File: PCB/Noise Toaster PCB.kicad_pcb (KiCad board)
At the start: 2 copper layers, 132.1 x 68.6 mm, 142 parts, among them J10 GND, J2 Power, J3 AREG, J4 LFO, J5 VCO, J6 VCO, J7 LPF, J8 VCA, J9 Amp, Q1 2N5457, Q10 2N3906, Q2 2N3904, Q3 2N3904, Q4 2N3904, Q5 2N3904, Q6 2N3904, Q7 2N5457, Q8 2N5457, Q9 2N5457, U1 LM324, U2 LM324, U3 LM386, X4 WNS

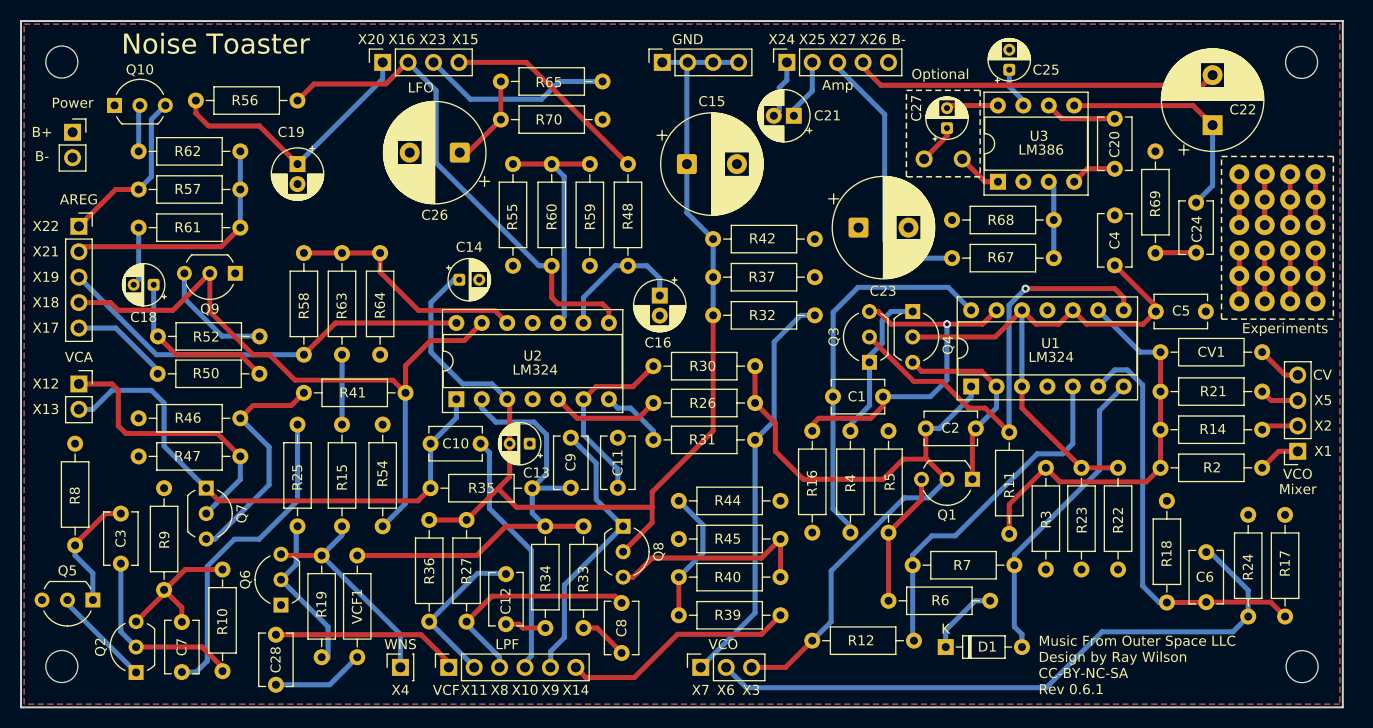
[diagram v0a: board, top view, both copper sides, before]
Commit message: Fixed grave mistake (Q10 position swapped)
Tom forgot to mirror Q10, swapping the emitter and collectors of Q10
Changed all the footprints of electrolytic caps to 5mm (i didnt find a single cap in my parts bin rated for 25V that was 4mm diameter)
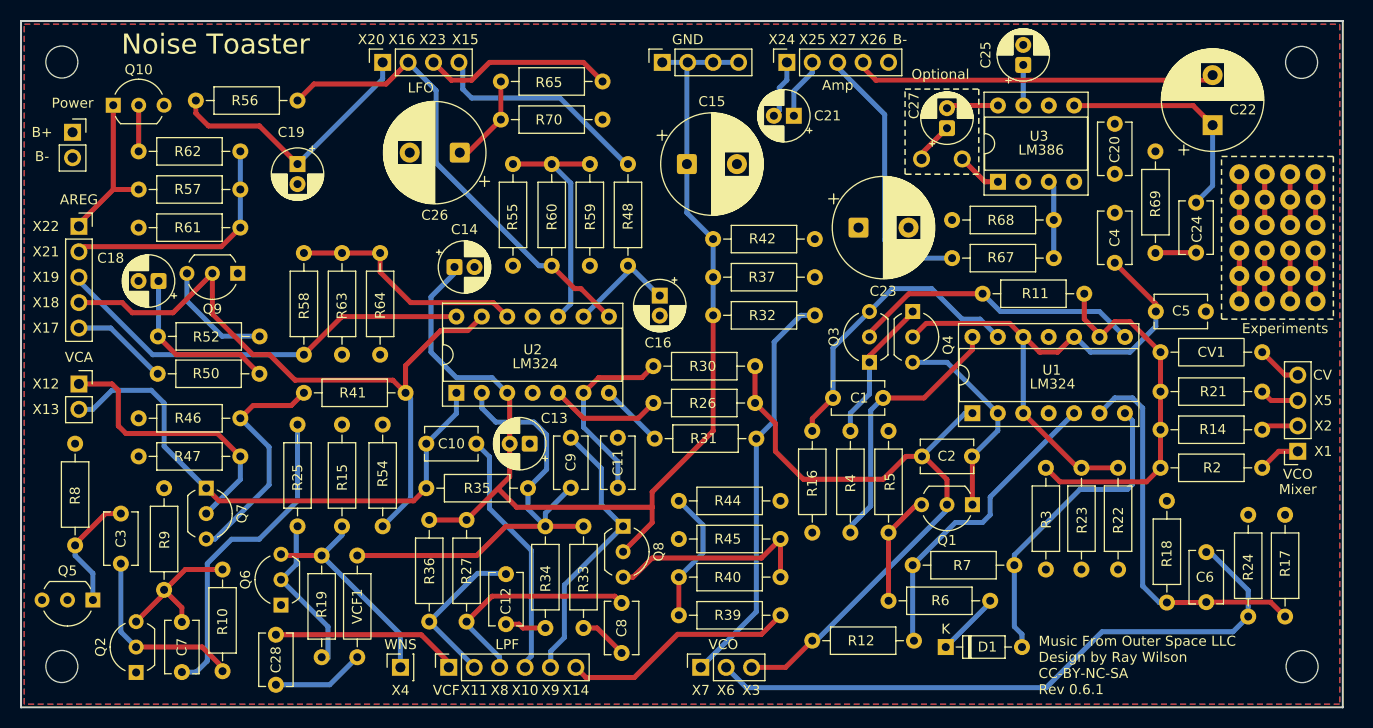
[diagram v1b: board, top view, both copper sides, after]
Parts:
- C13, C14, C18, C25, C27: footprint Capacitor_THT:CP_Radial_D4.0mm_P2.00mm -> Capacitor_THT:CP_Radial_D5.0mm_P2.00mm
- C2: value 0.001 uF -> 1 nF
- moved R11 25.1 mm to (181.5, 102.5), turned to 180 degrees
- moved C1 5.00 mm to (156.4, 112.9), turned to 0 degrees
- moved C2 2.82 mm to (170.3, 118.8)
- moved U1 2.67 mm to (170.3, 114.5)
- moved Q1 2.54 mm to (170.3, 123.6)
- moved C25 1.48 mm to (175.4, 79.7)
- moved C14 1.36 mm to (118.6, 99.8)
- moved U2 0.64 mm to (118.8, 112.4)
- moved C18 0.62 mm to (89.0, 101.2)
- moved C20 0.51 mm to (184.6, 90.5)
- moved C10 0.43 mm to (120.8, 117.5)
- moved R35 0.43 mm to (115.8, 121.9)
- moved C4 0.25 mm to (184.6, 99.4)
- moved Q9 0.25 mm to (96.9, 100.5)
- moved ? 0.25 mm to (165.3, 89.1)
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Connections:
- Q10 pad 1: B- -> /Attack Release Envelope Generator/X22
- Q10 pad 3: /Attack Release Envelope Generator/X22 -> B-
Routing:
- net B-: track 20.2 -> 0.00 mm
- net Net-(Q3-B): track 44.4 -> 29.3 mm, vias 1 -> 0
- net B+: track 14.1 -> 0.00 mm
- net Net-(C1-Pad2): track 37.9 -> 26.6 mm
- net Net-(Q3-C): track 35.2 -> 30.2 mm, vias 1 -> 0
- net /RMP: track 69.5 -> 65.3 mm
- net Net-(U1B-+): track 34.8 -> 30.9 mm
- net Net-(U1C--): track 40.2 -> 37.1 mm
- net /Front Panel/B: track 50.3 -> 47.5 mm
- net Net-(U1B--): track 41.2 -> 38.5 mm
- net Net-(U2C--): track 13.7 -> 11.1 mm
- net Net-(Q1-G): track 13.5 -> 11.3 mm
- net /Front Panel/X15: track 21.0 -> 22.5 mm
- net Net-(U2A--): track 46.4 -> 47.8 mm
- net Net-(Q3-E): track 15.1 -> 13.9 mm
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
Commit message: Final Update
Move power pins closer to filter caps
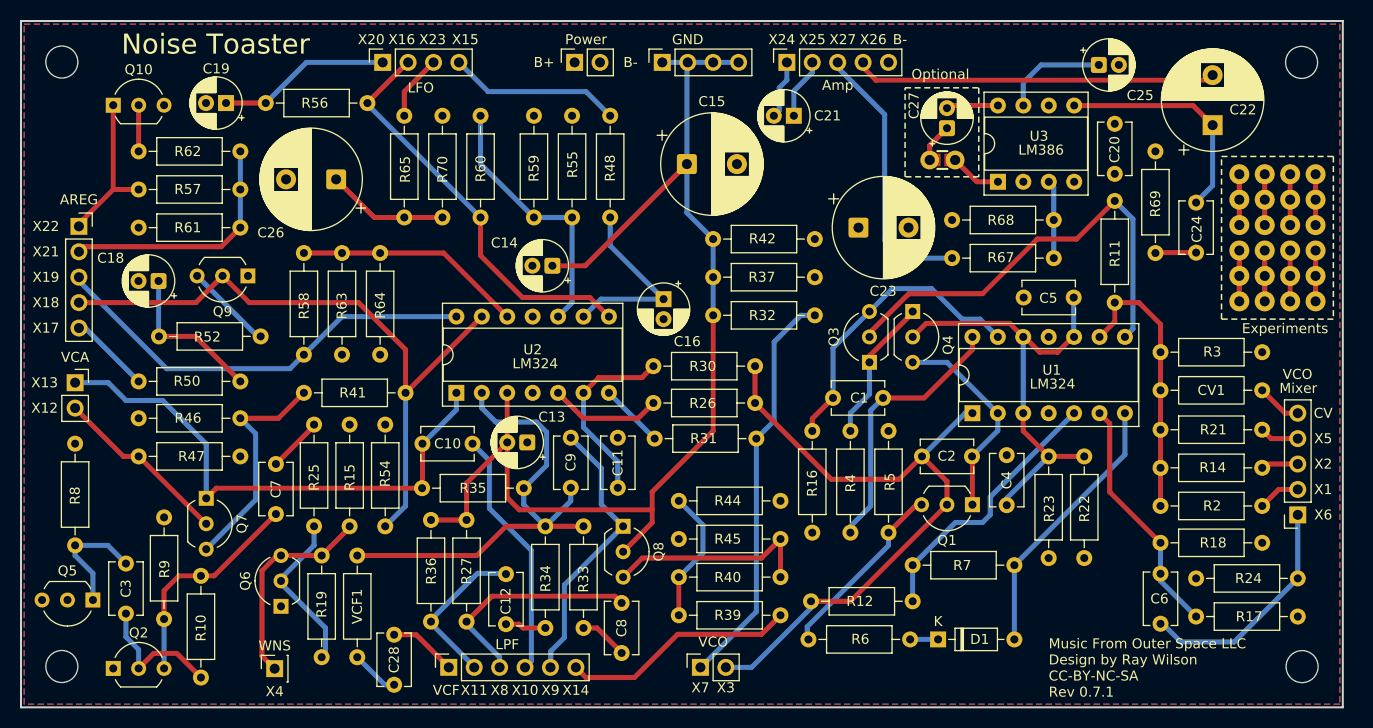
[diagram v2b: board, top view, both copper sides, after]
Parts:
- removed the ? at (169.3, 89.1)
- removed the ? at (165.3, 89.1)
- added JP1: Jumper_Measure_Open, PCM_SparkFun-Jumper:Jumper_2_PTH_SMD_Combo-NO, F.Cu at (167.3, 89.2)
- J5: footprint Connector_PinSocket_2.54mm:PinSocket_1x04_P2.54mm_Vertical -> Connector_PinSocket_2.54mm:PinSocket_1x05_P2.54mm_Vertical
- J6: footprint Connector_PinSocket_2.54mm:PinSocket_1x03_P2.54mm_Vertical -> Connector_PinSocket_2.54mm:PinSocket_1x02_P2.54mm_Vertical
- moved J2 50.6 mm to (130.6, 79.4), turned to 90 degrees
- moved C4 26.5 mm to (173.8, 123.6)
- moved R65 16.7 mm to (113.6, 94.9), turned to 90 degrees
- moved R3 16.3 mm to (189.1, 108.4), turned to 0 degrees
- moved R55 16.1 mm to (130.3, 84.7), turned to -90 degrees
- moved C7 14.3 mm to (100.7, 124.5), turned to 90 degrees
- moved C26 12.6 mm to (106.8, 91.1)
- moved X4 12.6 mm to (100.6, 140.0)
- moved C28 11.8 mm to (112.6, 141.6)
- moved R70 11.4 mm to (117.4, 94.9), turned to 90 degrees
- moved R47 10.2 mm to (87.0, 118.8), turned to 0 degrees
- moved C14 9.79 mm to (128.4, 99.7), turned to 180 degrees
- moved C19 9.39 mm to (95.8, 83.5), turned to 180 degrees
- moved R17 8.89 mm to (192.7, 134.8), turned to 0 degrees
- moved R6 8.88 mm to (154.0, 137.1)
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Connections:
- C27 pad 1: Net-(C27-Pad1) -> Net-(JP1-A)
- CV1 pad 2: Net-(J5-Pin_4) -> Net-(J5-Pin_5)
- J5 pad 1: /Front Panel/X1 -> /Front Panel/X6
- J5 pad 2: /Front Panel/X2 -> /Front Panel/X1
- J5 pad 3: /Front Panel/X5 -> /Front Panel/X2
- J5 pad 4: Net-(J5-Pin_4) -> /Front Panel/X5
- J6 pad 2: /Front Panel/X6 -> /RMP
- J8 pad 1: /Front Panel/X12 -> /FO
- J8 pad 2: /FO -> /Front Panel/X12
- U3 pad 1: Net-(C27-Pad1) -> Net-(JP1-B)
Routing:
- net /Front Panel/X6: track 64.0 -> 23.2 mm
- net Net-(C7-Pad2): track 32.0 -> 5.39 mm
- net Net-(Q3-B): track 29.3 -> 44.7 mm
- net Net-(U1B--): track 38.5 -> 24.3 mm
- net /Front Panel/X23: track 19.2 -> 6.54 mm
- net Net-(J7-Pin_1): track 18.4 -> 6.81 mm
- net /Front Panel/X12: track 28.3 -> 17.9 mm
- net /G2: track 55.9 -> 45.7 mm
- net /Front Panel/X20: track 27.2 -> 17.3 mm
- net Net-(U1C--): track 37.1 -> 27.7 mm
- net Net-(C27-Pad1): track 8.64 -> 0.00 mm
- net Net-(U2C--): track 11.1 -> 19.1 mm
- net Net-(Q2-C): track 14.6 -> 22.1 mm
- net Net-(Q1-G): track 11.3 -> 18.4 mm
- net Net-(U3-BYPASS): track 4.06 -> 10.6 mm
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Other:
- board text added: "Music From Outer Space LLC Design by Ray Wilson CC-BY-NC-SA Rev 0.7.1"
- board text removed: "Music From Outer Space LLC Design by Ray Wilson CC-BY-NC-SA Rev 0.6.1"
